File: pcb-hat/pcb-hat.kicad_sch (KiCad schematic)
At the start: 58 parts, among them Q1 NTMFS5C468NLT1G, Q2 Q_PMOS_GSD, U1 HTD Servo, U2 INA219AxD, U3 AOZ6605PI-1, U4 Vertical_Pi_Breakout, U5 Power_Connector, U6 Horizontal_Pi_Breakout, U7 AOZ6605PI-1, U8 Raspberry_Pi_Generic

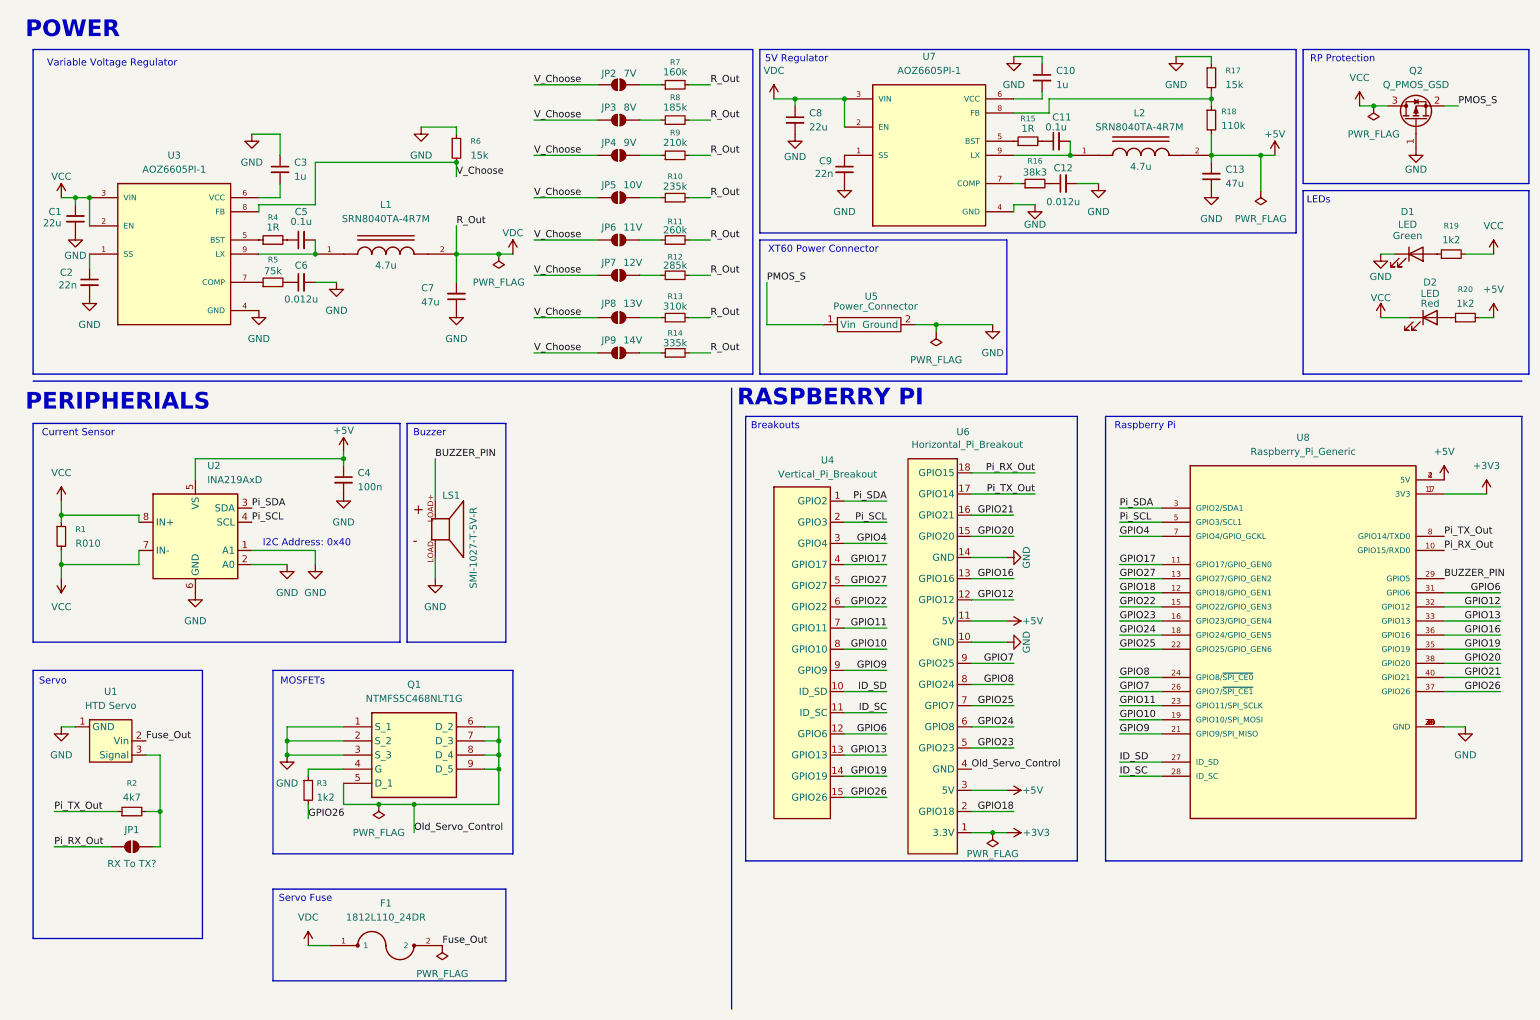
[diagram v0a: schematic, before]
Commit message: Finish LED circuitry
Involves anti parallel LEDs and a NPN Transistor to control voltage received on the blue led
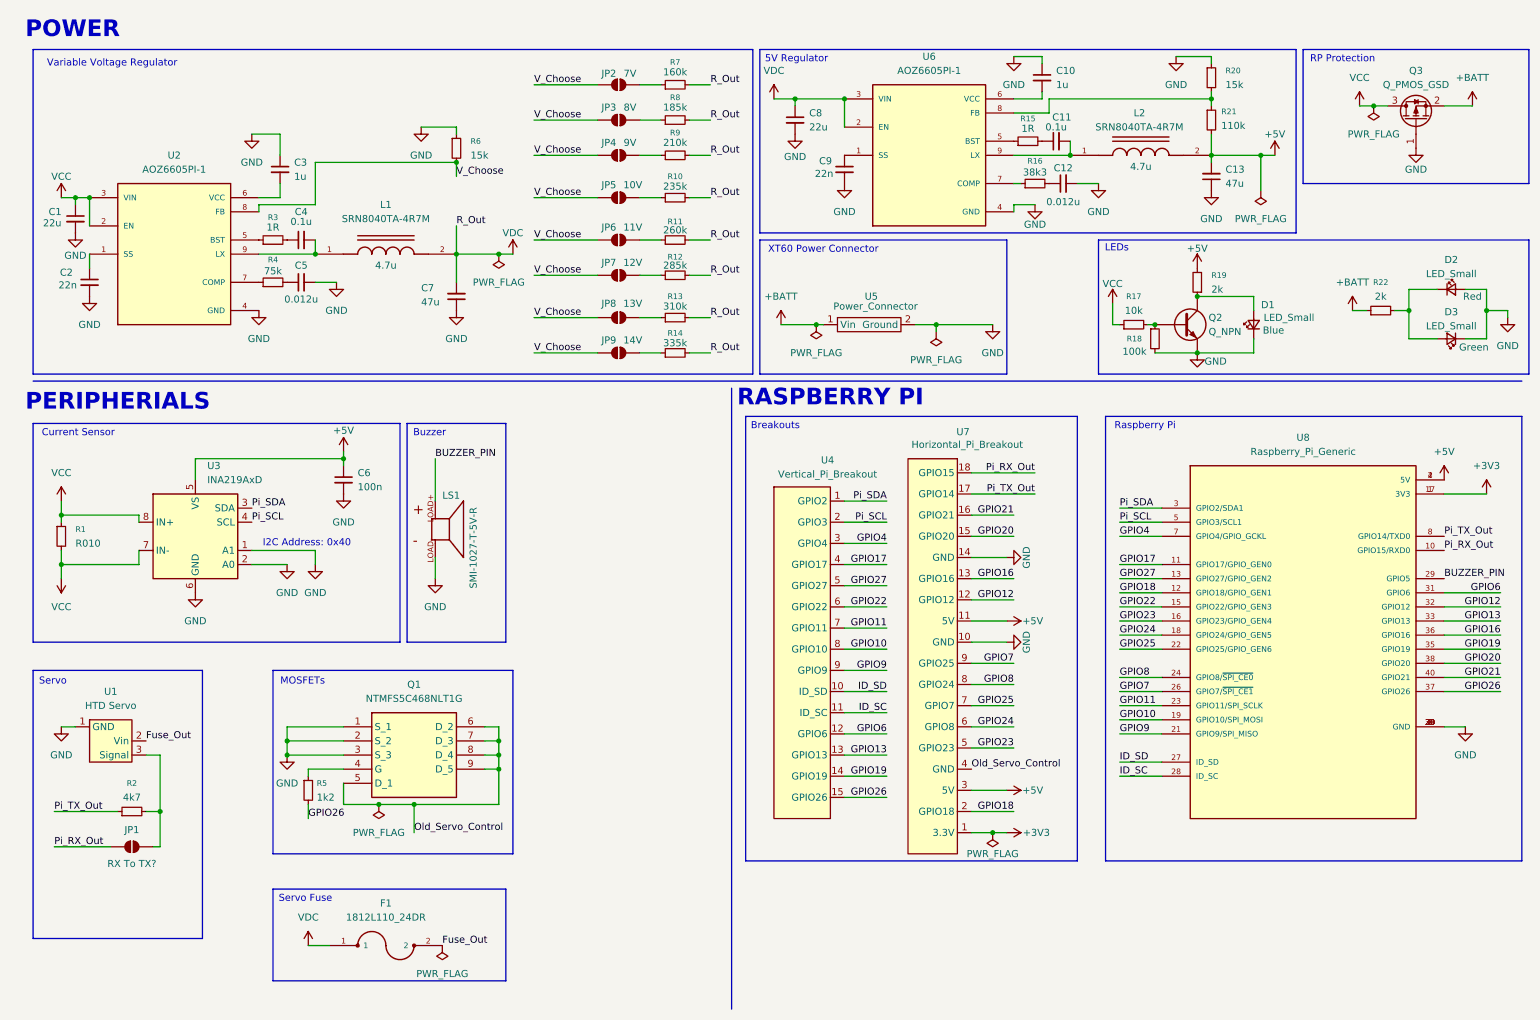
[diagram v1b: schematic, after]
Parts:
- removed D1, D2: LED, symbol Device:LED
- removed R19: 1k2, Resistor_SMD:R_0603_1608Metric_Pad0.98x0.95mm_HandSolder, symbol Device:R_Small
- added D1: LED_Small, pcb_hat:LEDC1608X35N, symbol Device:LED_Small
- added D2: LED_Small, pcb_hat:LEDLSQ97601N1Q21, symbol Device:LED_Small
- added D3: LED_Small, pcb_hat:LEDM1608X80, symbol Device:LED_Small
- added Q2: Q_NPN, pcb_hat:MTR_MMBT2222A-TP_MCE, symbol Device:Q_NPN
- added R17: 10k, Resistor_SMD:R_0603_1608Metric_Pad0.98x0.95mm_HandSolder, symbol Device:R_Small
- added R18: 100k, Resistor_SMD:R_0603_1608Metric_Pad0.98x0.95mm_HandSolder, symbol Device:R_Small
- added R22: 2k, Resistor_SMD:R_0603_1608Metric_Pad0.98x0.95mm_HandSolder, symbol Device:R_Small
- F1: Digikey Link (none) -> https://www.digikey.com/en/products/detail/littelfuse-inc/1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
- R19: renamed from R20; value 1k2 -> 2k; Digikey Link (none) -> https://www.digikey.com/en/products/detail/panasonic-electr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
- renumbered C5 to C4, C6 to C5, C4 to C6, Q2 to Q3, R17 to R20, R18 to R21, R4 to R3, R5 to R4, R3 to R5, U3 to U2, U2 to U3, U7 to U6, U6 to U7
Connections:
- net GND: now also D1.1 (K), D2.2 (A), D3.1 (K), Q2.E, R18.2
- net VCC: now also R17.1
- net at R19.1: now also D1.2 (A), Q2.C
- net PMOS_S renamed +BATT
- net +BATT: now also R22.1
- new net: Q2.B, R17.2, R18.1
- new net: D2.1 (K), D3.2 (A), R22.2
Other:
- moved on the sheet: R19

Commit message: More net classes, fix 2 major bugs with current sensor wiring
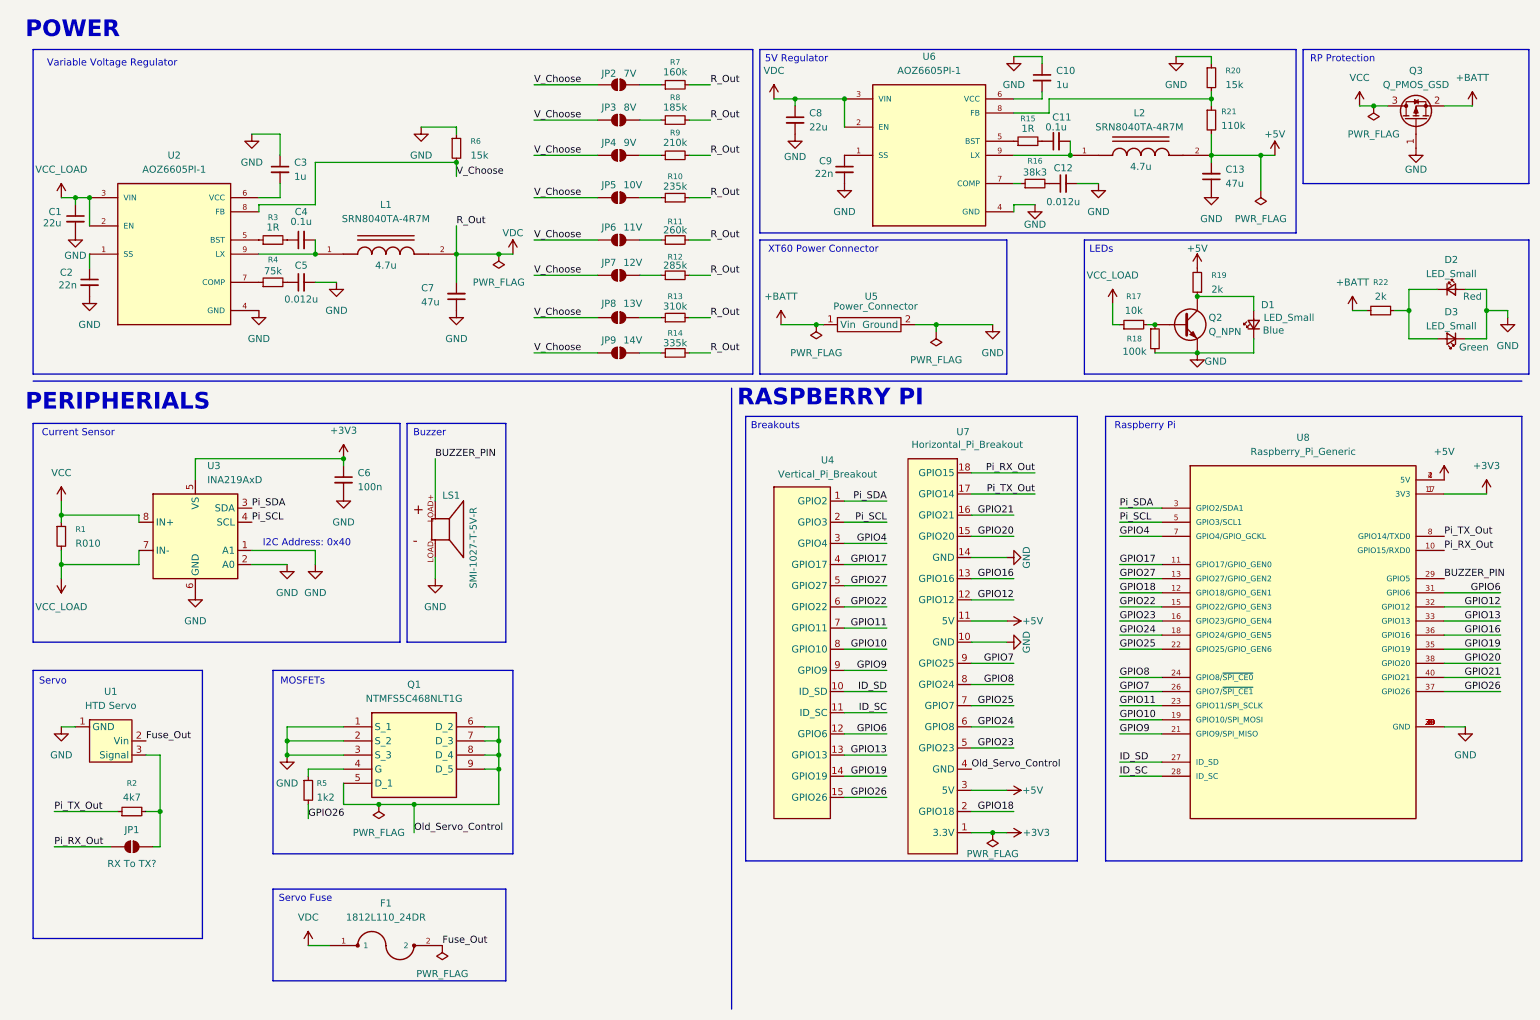
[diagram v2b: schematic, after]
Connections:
- net +3V3: now also C6.1, U3.5 (VS)
- net +5V: no longer C6.1, U3.5 (VS)
- net VCC: no longer C1.1, R1.2, R17.1, U2.2 (EN), U2.3 (VIN), U3.7 (IN-)
- new net VCC_LOAD: C1.1, R1.2, R17.1, U2.2 (EN), U2.3 (VIN), U3.7 (IN-)

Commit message: Finish Schematic
Add a switch and combine the 2 servos into one
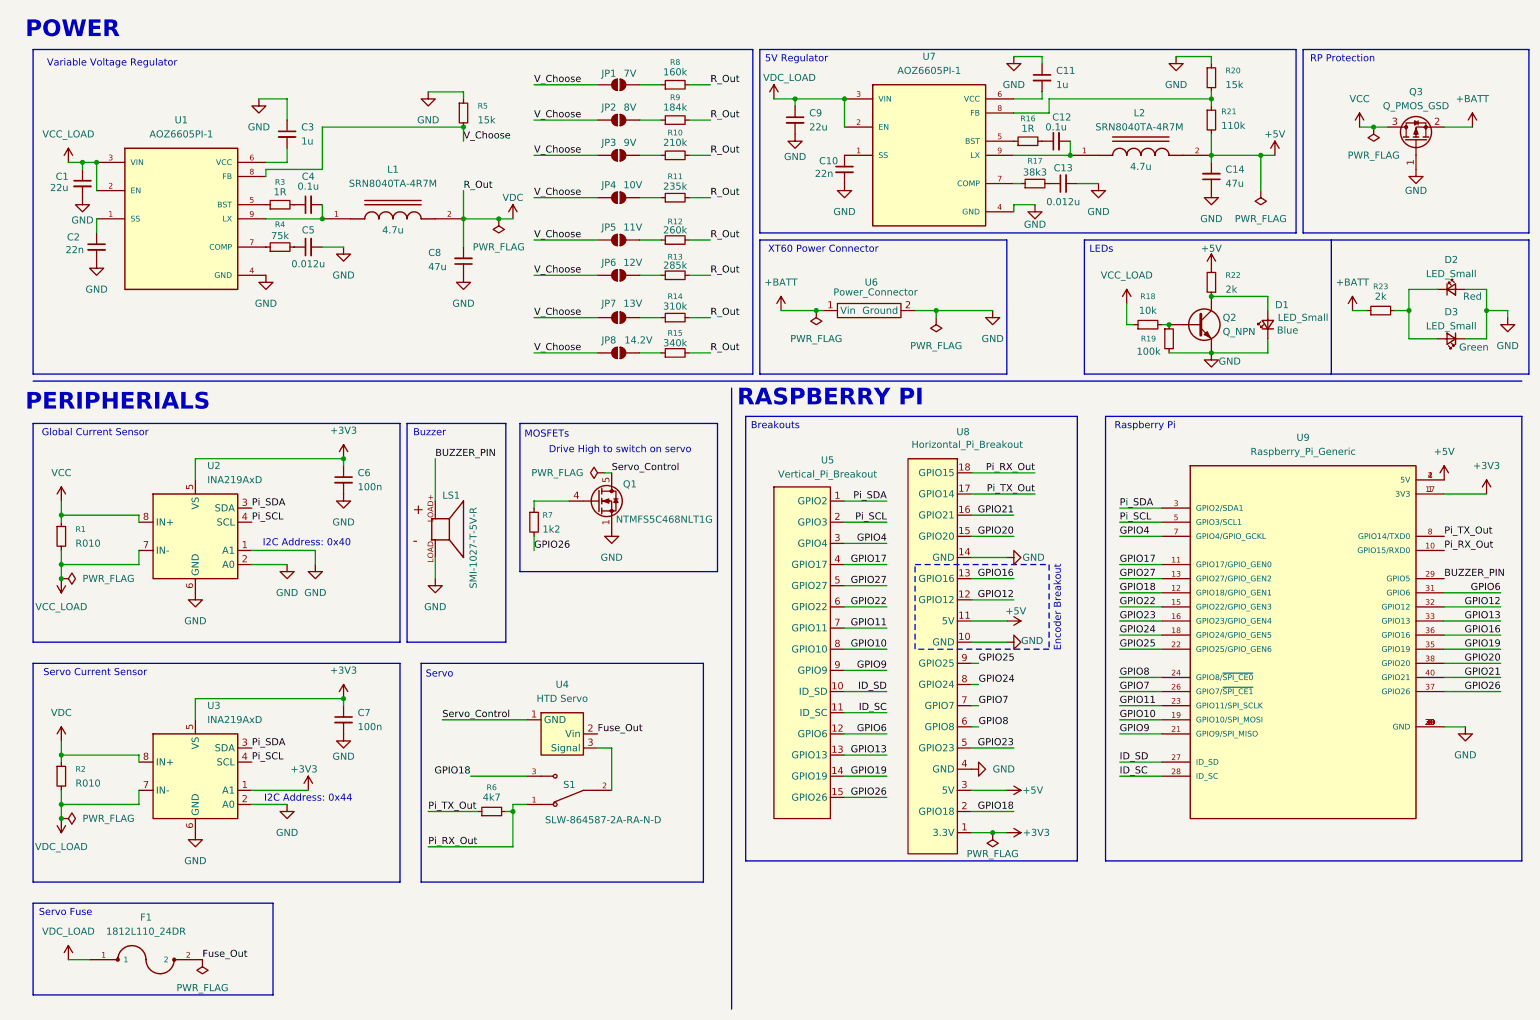
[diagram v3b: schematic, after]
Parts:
- removed JP1: SolderJumper_2_Open, Jumper:SolderJumper-2_P1.3mm_Open_RoundedPad1.0x1.5mm, symbol Jumper:SolderJumper_2_Open
- removed Q1: NTMFS5C468NLT1G, pcb_hat:NRVTS10100EMFST1G, symbol PiHatComponents:NTMFS5C468NLT1G
- added C7: 100n, Capacitor_SMD:C_0603_1608Metric_Pad1.08x0.95mm_HandSolder, symbol Device:C_Small
- added Q1: NTMFS5C468NLT1G, pcb_hat:NRVTS10100EMFST1G, symbol PiHatComponents:NMOS_SERVO_CUTOFF
- added R2: R010, Resistor_SMD:R_0603_1608Metric, symbol Device:R_Small
- added S1: SLW-864587-2A-RA-N-D, pcb_hat:SW_SLW-864587-2A-RA-N-D, symbol PiHatComponents:SLW-864587-2A-RA-N-D
- added U3: INA219AxD, Package_SO:SOIC-8_3.9x4.9mm_P1.27mm, symbol Sensor_Energy:INA219AxD
- C1: Digikey PN (none) -> CL10A226MP8NUNE
- C10: renamed from C9; Digikey https://www.digikey.com/en/products/detail/nextgen-componen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 -> (none); Digikey PN (none) -> CGA3E2X7R1H223K080AA
- C11: renamed from C10; Digikey https://www.digikey.com/en/products/detail/nextgen-componen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 -> (none); Digikey PN (none) -> CL10B105KA8NNNC
- C12: renamed from C11; Digikey https://www.digikey.com/en/products/detail/nextgen-componen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 -> (none); Digikey PN (none) -> C0603C104K3RACTU
- C13: renamed from C12; Digikey https://www.digikey.com/en/products/detail/yageo/CC0603JRX7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 -> (none); Digikey PN (none) -> CC0603JRX7R8BB123
- C14: renamed from C13; Digikey https://www.digikey.com/en/products/detail/tdk-corporation/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 -> (none); Digikey PN (none) -> C3216X5R1E476M160AC
- C2: Digikey https://www.digikey.com/en/products/detail/nextgen-componen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 -> (none); Digikey PN (none) -> CGA3E2X7R1H223K080AA
- C3: Digikey https://www.digikey.com/en/products/detail/nextgen-componen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 -> (none); Digikey PN (none) -> CL10B105KA8NNNC
- C4, C6: Digikey https://www.digikey.com/en/products/detail/nextgen-componen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 -> (none); Digikey PN (none) -> C0603C104K3RACTU
- C5: Digikey https://www.digikey.com/en/products/detail/yageo/CC0603JRX7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 -> (none); Digikey PN (none) -> CC0603JRX7R8BB123
- C8: renamed from C7; Digikey https://www.digikey.com/en/products/detail/tdk-corporation/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 -> (none); Digikey PN (none) -> C3216X5R1E476M160AC
- C9: renamed from C8; Digikey PN (none) -> CL10A226MP8NUNE
- D1: Digikey Link https://www.digikey.com/en/products/detail/liteon/LTST-C194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 -> (none); Digikey PN (none) -> LTST-C194TBKT
- D2: Digikey Link https://www.digikey.com/en/products/detail/ams-osram-usa-in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 -> (none); Digikey PN (none) -> LS Q976.01-N1Q2-1-20-R18
- D3: Digikey Link https://www.digikey.com/en/products/detail/liteon/LTST-C190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 -> (none); Digikey PN (none) -> LTST-C190GKT
- F1: Digikey Link https://www.digikey.com/en/products/detail/littelfuse-inc/1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 -> (none); Digikey PN (none) -> 1812L110-24DR
- JP8: renamed from JP9; V_out 14V -> 14.2V
- L1, L2: Digikey PN (none) -> SRN8040TA-4R7M
- LS1: Digikey Link https://www.digikey.com/en/products/detail/pui-audio-inc/sm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 -> (none); Digikey PN (none) -> smi-1027-t-5v-r
- Q2: Digikey Link https://www.digikey.com/en/products/detail/mcc-micro-commer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 -> (none); Digikey PN (none) -> MMBT2222A-TP
- Q3: Digikey Link https://www.digikey.com/en/products/detail/vishay-siliconix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 -> (none); Digikey PN (none) -> si2347ds-t1-ge3
- R1: Digikey https://www.digikey.com/en/products/detail/yageo/PE0603FRE5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 -> (none); Digikey PN (none) -> PE0603FRE570R01Z
- R10: renamed from R9; Digikey PN (none) -> CRCW0603210KFKEA
- R11: renamed from R10; Digikey PN (none) -> RT0603DRE07234KL
- R12: renamed from R11; Digikey PN (none) -> RC0603FR-07261KL
- R13: renamed from R12; Digikey PN (none) -> RR0816P-2843-D-E00
- R14: renamed from R13; Digikey PN (none) -> CRCW0603309KFKEA
- R15: renamed from R14; value 335k -> 340k; Digikey PN (none) -> RC0603FR-07340KL
- R16: renamed from R15; Digikey https://www.digikey.com/en/products/detail/panasonic-electr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 -> (none); Digikey PN (none) -> ERJ-UP3J1R0V
- R17: renamed from R16; Digikey https://www.digikey.com/en/products/detail/yageo/RC0603FR-0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 -> (none); Digikey PN (none) -> RC0603FR-0738K3L
- R18: renamed from R17; Digikey PN (none) -> RC0603FR-0710KL
- R19: renamed from R18; Digikey PN (none) -> RC0603FR-07100KL
- R20: Digikey https://www.digikey.com/en/products/detail/vishay-dale/CRCW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 -> (none); Digikey PN (none) -> CRCW060315K0FKEA
- R21: Digikey Link https://www.digikey.com/en/products/detail/vishay-dale/CRCW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 -> (none); Digikey PN (none) -> CRCW0603110KFKEAC
- R22: renamed from R19; Digikey Link https://www.digikey.com/en/products/detail/panasonic-electr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 -> (none); Digikey PN (none) -> ERJ-PA3J202V
- R23: renamed from R22; Digikey Link https://www.digikey.com/en/products/detail/panasonic-electr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 -> (none); Digikey PN (none) -> ERJ-PA3J202V
- R3: Digikey https://www.digikey.com/en/products/detail/panasonic-electr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 -> (none); Digikey PN (none) -> ERJ-UP3J1R0V
- R4: Digikey https://www.digikey.com/en/products/detail/rohm-semiconduct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 -> (none); Digikey PN (none) -> ESR03EZPJ753
- R5: renamed from R6; Digikey https://www.digikey.com/en/products/detail/vishay-dale/CRCW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 -> (none); Digikey PN (none) -> CRCW060315K0FKEA
- R6: renamed from R2; Digikey PN (none) -> RC0603FR-074K7L
- R7: renamed from R5; Digikey Link https://www.digikey.com/en/products/detail/panasonic-electr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 -> (none); Digikey PN (none) -> ERA-3AEB122V
- R8: renamed from R7; Digikey PN (none) -> CRCW0603160KFKEA
- R9: renamed from R8; value 185k -> 184k; Digikey PN (none) -> RN73R1JTTD1840B25
- U1: renamed from U2; Availability In Stock -> (none); Check_prices https://www.snapeda.com/parts/AOZ6605PI-1/Alpha/view-part/?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 -> (none); Description_1 Buck Switching Regulator IC Positive Adjustable 0.8V 1 Outp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 -> (none); Digikey PN (none) -> AOZ6605PI-1; MANUFACTURER Alpha and Omega Semiconductor -> (none); MAXIMUM_PACKAGE_HEIGHT 1.7mm -> (none); MF Alpha & Omega Semiconductor Inc. -> (none); MP AOZ6605PI-1 -> (none); PARTREV 1.1 -> (none); Package SOIC-8 Alpha &amp; Omega Semiconductor Inc. -> (none); Price None -> (none); STANDARD IPC 7351B -> (none)
- U2: renamed from U3; Digikey PN (none) -> INA219AIDR
- U4: renamed from U1; now left out of the parts list
- U5: renamed from U4; now left out of the parts list
- U6: renamed from U5; now left out of the parts list
- U7: renamed from U6; Availability In Stock -> (none); Check_prices https://www.snapeda.com/parts/AOZ6605PI-1/Alpha/view-part/?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 -> (none); Description_1 Buck Switching Regulator IC Positive Adjustable 0.8V 1 Outp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 -> (none); Digikey PN (none) -> AOZ6605PI-1; MANUFACTURER Alpha and Omega Semiconductor -> (none); MAXIMUM_PACKAGE_HEIGHT 1.7mm -> (none); MF Alpha & Omega Semiconductor Inc. -> (none); MP AOZ6605PI-1 -> (none); PARTREV 1.1 -> (none); Package SOIC-8 Alpha &amp; Omega Semiconductor Inc. -> (none); Price None -> (none); STANDARD IPC 7351B -> (none)
- U8: renamed from U7; now left out of the parts list
- U9: renamed from U8; now left out of the parts list
- renumbered JP2 to JP1, JP3 to JP2, JP4 to JP3, JP5 to JP4, JP6 to JP5, JP7 to JP6, JP8 to JP7
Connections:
- net Old_Servo_Control is gone; now on net GND: U8.4 (GND)
- net +3V3: now also C7.1, U3.1 (A1), U3.5 (VS)
- net GND: now also C7.2, Q1.1 (S), Q1.2 (S), Q1.3 (S), U3.2 (A0), U3.6 (GND); no longer U4.1 (GND)
- net GPIO18: now also S1.3
- net GPIO24: now also U8.8 (GPIO24); no longer U8.6 (GPIO8)
- net GPIO25: now also U8.9 (GPIO25); no longer U8.7 (GPIO7)
- net GPIO7: now also U8.7 (GPIO7); no longer U8.9 (GPIO25)
- net GPIO8: now also U8.6 (GPIO8); no longer U8.8 (GPIO24)
- net Pi_RX_Out: now also R6.2, S1.1
- net Pi_SCL: now also U3.4 (SCL)
- net Pi_SDA: now also U3.3 (SDA)
- net VDC: now also R2.1, U3.8 (IN+); no longer C9.1, F1.1, U7.2 (EN), U7.3 (VIN)
- net at U4.3 (Signal): now also S1.2; no longer R6.2
- net at R7.1: now also Q1.4 (G)
- new net Servo_Control: Q1.5 (D), Q1.6 (D), Q1.7 (D), Q1.8 (D), Q1.9 (D), U4.1 (GND)
- new net VDC_LOAD: C9.1, F1.1, R2.2, U3.7 (IN-), U7.2 (EN), U7.3 (VIN)
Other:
- note added: "Drive High to switch on servo"
- note added: "Encoder Breakout"
- note added: "Global Current Sensor"
- note added: "I2C Address: 0x44"
- note added: "Servo Current Sensor"
- note removed: "Current Sensor"
- moved on the sheet: C1, C2, C3, C4, C5, C8, D1, F1, L1, Q2, Q3, R18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
